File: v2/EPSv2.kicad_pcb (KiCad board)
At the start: 4 copper layers, 50 x 110 mm, 174 parts, among them J1 Conn_01x03, J10 Conn_01x05_Pin, J2 Conn_01x03, J3 Conn_01x02, J4 5037630491, J5 2P 21700 Cell Holder, J6 5037630491, J7 1053091102, J8 1053091102, J9 1053091102, Q1 AO3400A, Q2 AO3400A, Q3 AO3400A, Q4 AO3400A, Q5 AP25P06K, Q6 AP25P06K, Q7 AP25P06K, U1 BQ29700DSER, U10 TPS63070RNMR, U11 LM73100RPWR, U12 LM73100RPWR, U13 TPS63070RNMR, U14 ISO1044BD, U2 BQ29700DSER, U3 MCP73831T-2ACI/OT, U4 MCP73831T-2ACI/OT, U5 LM73100RPWR, U6 C3235556 (M66200DRLR), U7 C3235556 (M66200DRLR), U8 STM32L432KCUx, U9 TPS63070RNMR

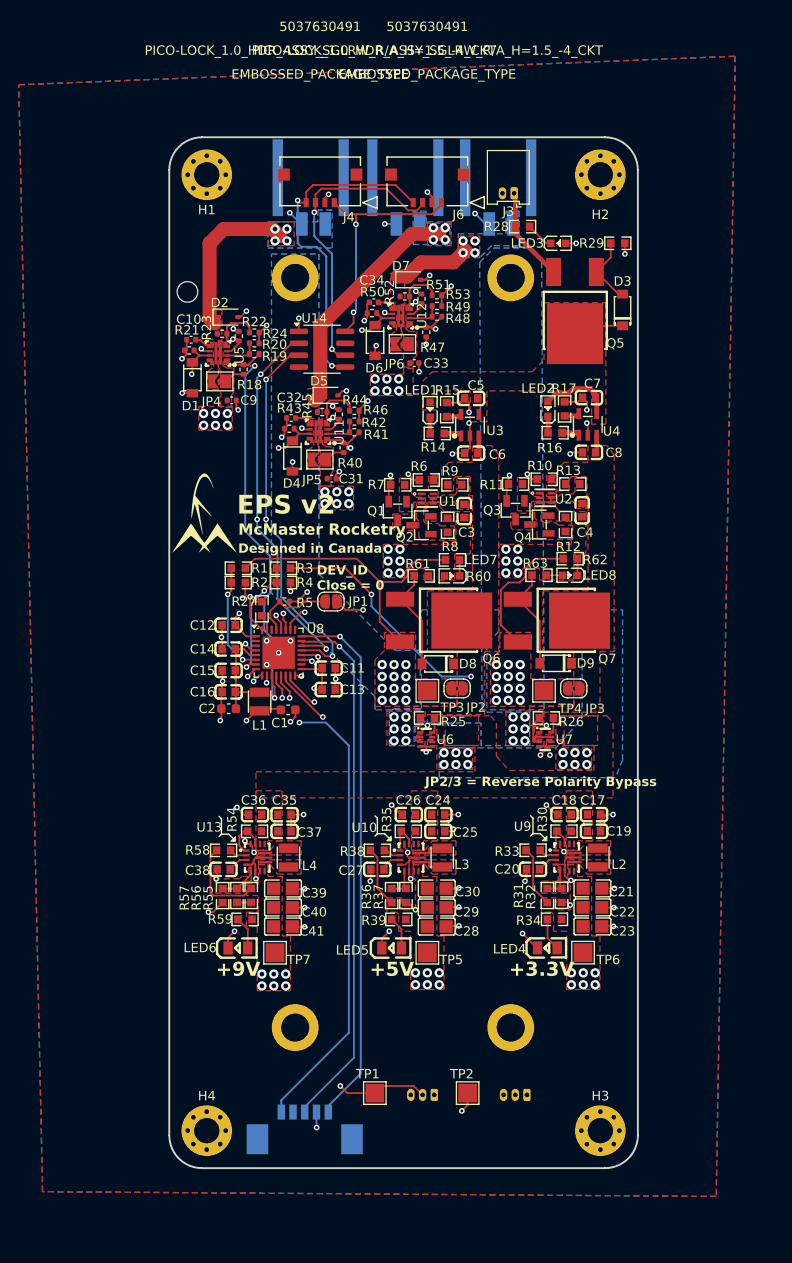
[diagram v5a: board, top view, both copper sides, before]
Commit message: load switch default OFF
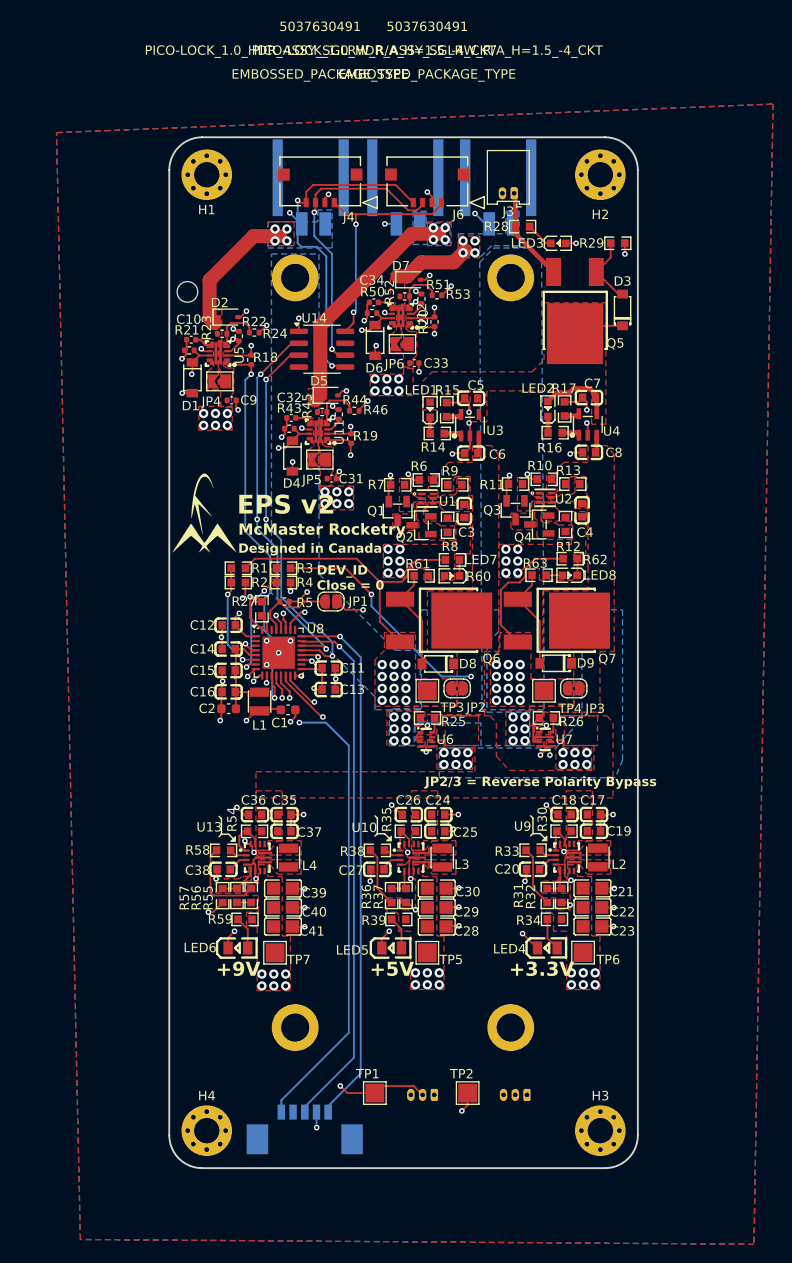
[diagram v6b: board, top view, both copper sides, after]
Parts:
- removed R40, R47: 470k, Resistor_SMD:R_0402_1005Metric
- removed R41, R48: 220k, Resistor_SMD:R_0402_1005Metric
- removed R42, R49: 100k, Resistor_SMD:R_0402_1005Metric
- R19: value 220k -> 470k
- R20: value 100k -> 470k
- moved R20 19.4 mm to (3.30, -35.3), turned to 90 degrees
- moved R19 13.7 mm to (-5.59, -22.9), turned to 90 degrees
- moved R18 1.30 mm to (-16.3, -31.2)
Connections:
- R18 pad 1: +9V -> ~{MCU_LS_1}
- R18 pad 2: ~{MCU_LS_1} -> GND
- R19 pad 1: ~{MCU_LS_1} -> ~{MCU_LS_2}
- R19 pad 2: Net-(U5-OVLO) -> GND
- R20 pad 1: Net-(U5-OVLO) -> ~{MCU_LS_3}
- U11 pad 2: Net-(U11-OVLO) -> GND
- U12 pad 2: Net-(U12-OVLO) -> GND
- U5 pad 2: Net-(U5-OVLO) -> GND
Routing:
- net GND: track 152.0 -> 159.3 mm, vias 86 -> 89
- net Net-(U11-OVLO): track 3.62 -> 0.00 mm
- net Net-(U12-OVLO): track 3.62 -> 0.00 mm
- net Net-(U5-OVLO): track 3.62 -> 0.00 mm
- net /LM7310_9V/VOUT: track 17.2 -> 14.3 mm
- net +5V: track 8.65 -> 6.52 mm
- net +9V: track 11.7 -> 9.57 mm
- net ~{MCU_LS_1}: track 44.9 -> 42.9 mm
- net ~{MCU_LS_3}: track 53.9 -> 52.2 mm
- net ~{MCU_LS_2}: track 39.9 -> 38.6 mm
- net +3.3V: track 27.5 -> 26.7 mm, vias 21 -> 20
- net /BQ29700_2/CELL+: vias 17 -> 12
- net /BQ29700_1/CELL+: vias 7 -> 12
